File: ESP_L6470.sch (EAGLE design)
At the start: 33 parts, among them J2 POWER_JACKPTH_LOCK, Q1 600mA/40V, Q2 600mA/40V, U1 L6470, U2 ESP-WROOM-03, U3 WS2811

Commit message: Update schematic with USB to Serial
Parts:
- removed U3: WS2811, SparkFun-LED:LED-TRICOLOR-5050-ICWS2811
- added C9: 10uF, microbuilder:CAP_CERAMIC0805-NOOUTLINE
- added D2: RED, microbuilder:LED0805_NOOUTLINE
- added D3: GREEN, microbuilder:LED0805_NOOUTLINE
- added IC2: CP2104, microbuilder:CP2104
- added JP2, JP3: JUMPER-SMT_2_NC_TRACE_NO-SILK, SparkFun-Jumpers:JUMPER-SMT_2_NC_TRACE_NO-SILK
- added R3, R4: 1K, microbuilder:RESISTOR0805_NOOUTLINE
- added X1: 20329, microbuilder:USB_MICRO_20329_V2
- C7: value 0.1uF -> 10uF; device SparkFun-Capacitors:0.1UF-25V(+80/-20%)(0603) -> microbuilder:CAP_CERAMIC0805-NOOUTLINE
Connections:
- net MC_EN renamed RESET
- new net N$1: U2.IO25
- new net N$10: U2.SDI
- new net N$13: IC2G$1.D+, X1.D+
- new net N$14: IC2G$1.D-, X1.D-
- new net N$15: C7.1, IC2G$1.VPP
- new net N$16: D2.A, R3.1
- new net N$17: D3.A, R4.1
- new net N$18: D2.C, IC2G$1.GPIO0/TXLED
- new net N$19: D3.C, IC2G$1.GPIO1/RXLED
- new net N$2: U2.SHD
- new net N$3: U2.SWP
- new net N$4: U2.SCS
- new net N$5: U2.SCK
- new net N$6: U2.SDO
- new net RXD0: IC2G$1.TXD, JP2.1
- new net TXD0: IC2G$1.RXD, JP3.1
- new net VBUS: IC2G$1.VBUS, X1.VBUS
- net 3.3V: now also C9.1, IC2G$1.REGIN, IC2G$1.VDD, IC2G$1.VIO, R3.2, R4.2; no longer C7.1, U3.VDD
- net DTR: now also IC2G$1.DTR
- net GND: now also C9.2, IC2G$1.GND, X1.GND; no longer U3.VSS
- net NEOPIXEL: no longer U3.DI
- net PGND: now also J2.GND, J2.GNDBREAK; no longer J2.PWR
- net RTS: now also IC2G$1.RTS
- net RX: now also JP3.2
- net TX: now also JP2.2
- net VS: now also J2.PWR; no longer J2.GND, J2.GNDBREAK
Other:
- note added: "CP2105 usb to serial"
- note added: "PHYSICAL INTERFACE"
- note added: "POWER JACK"
- note added: "TO STEPER"
- note added: "USB TO SERIAL CONVERTER"
- note removed: "INTERFACE"
- note removed: "SJ1 allows user to select external power over comm headers or internal 3.3V power. NB- DO NOT connect external power to JP1 or JP2 when internal supply is selected!"
- note removed: "SJ3 allows you to route the SDO (serial data out) either to the next board (if this board is in a chain) or back to the previous board (if this board is the last or only board in the chain). It defaults to back to previous board, for single board applications."
- note removed: "Supply Connector"
- note removed: "Vs must be between 8V and 45V Motor supply must be enabled for chip comms to work!"
- moved on the sheet: C7, J2, PROGRAMMER

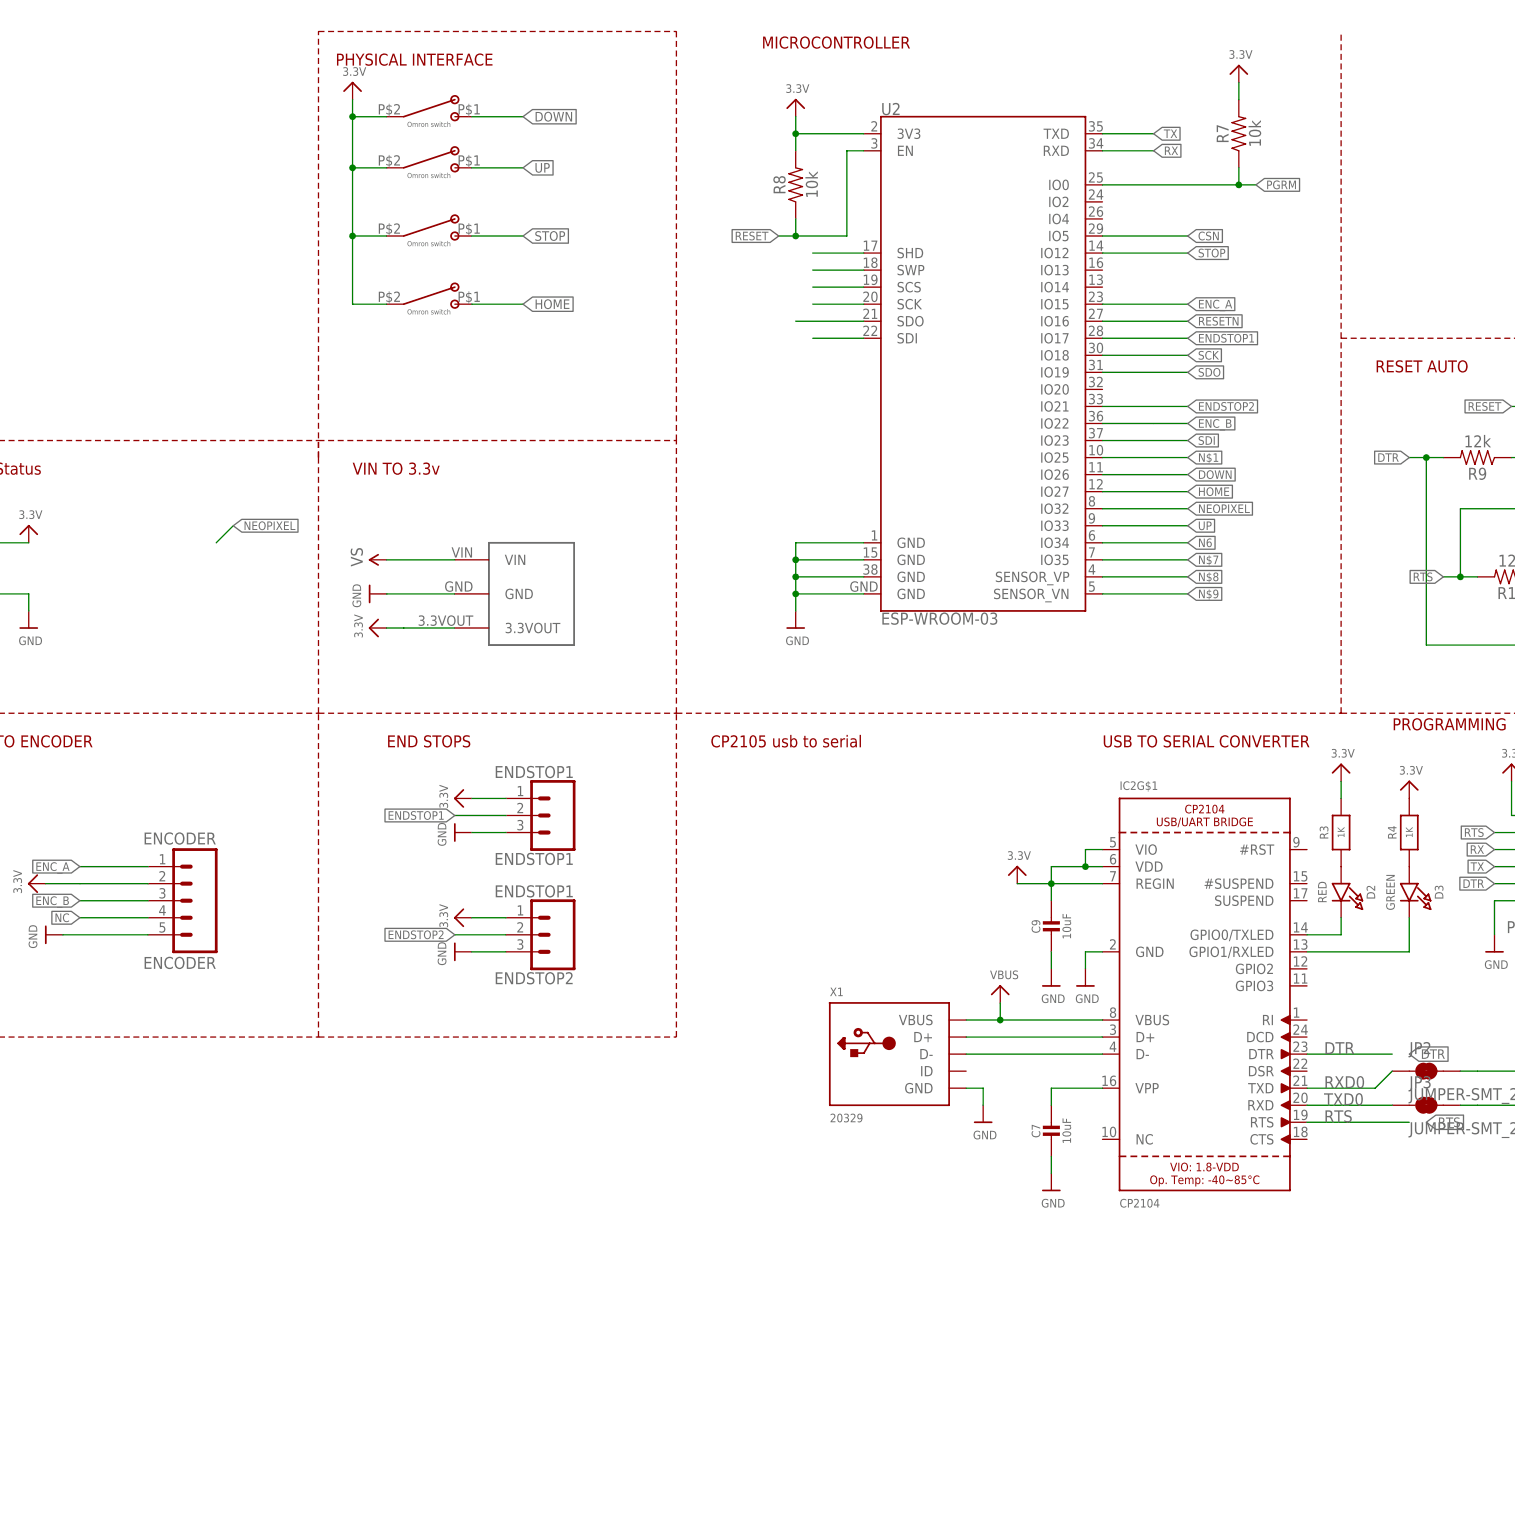
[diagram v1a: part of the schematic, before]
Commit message: added some components
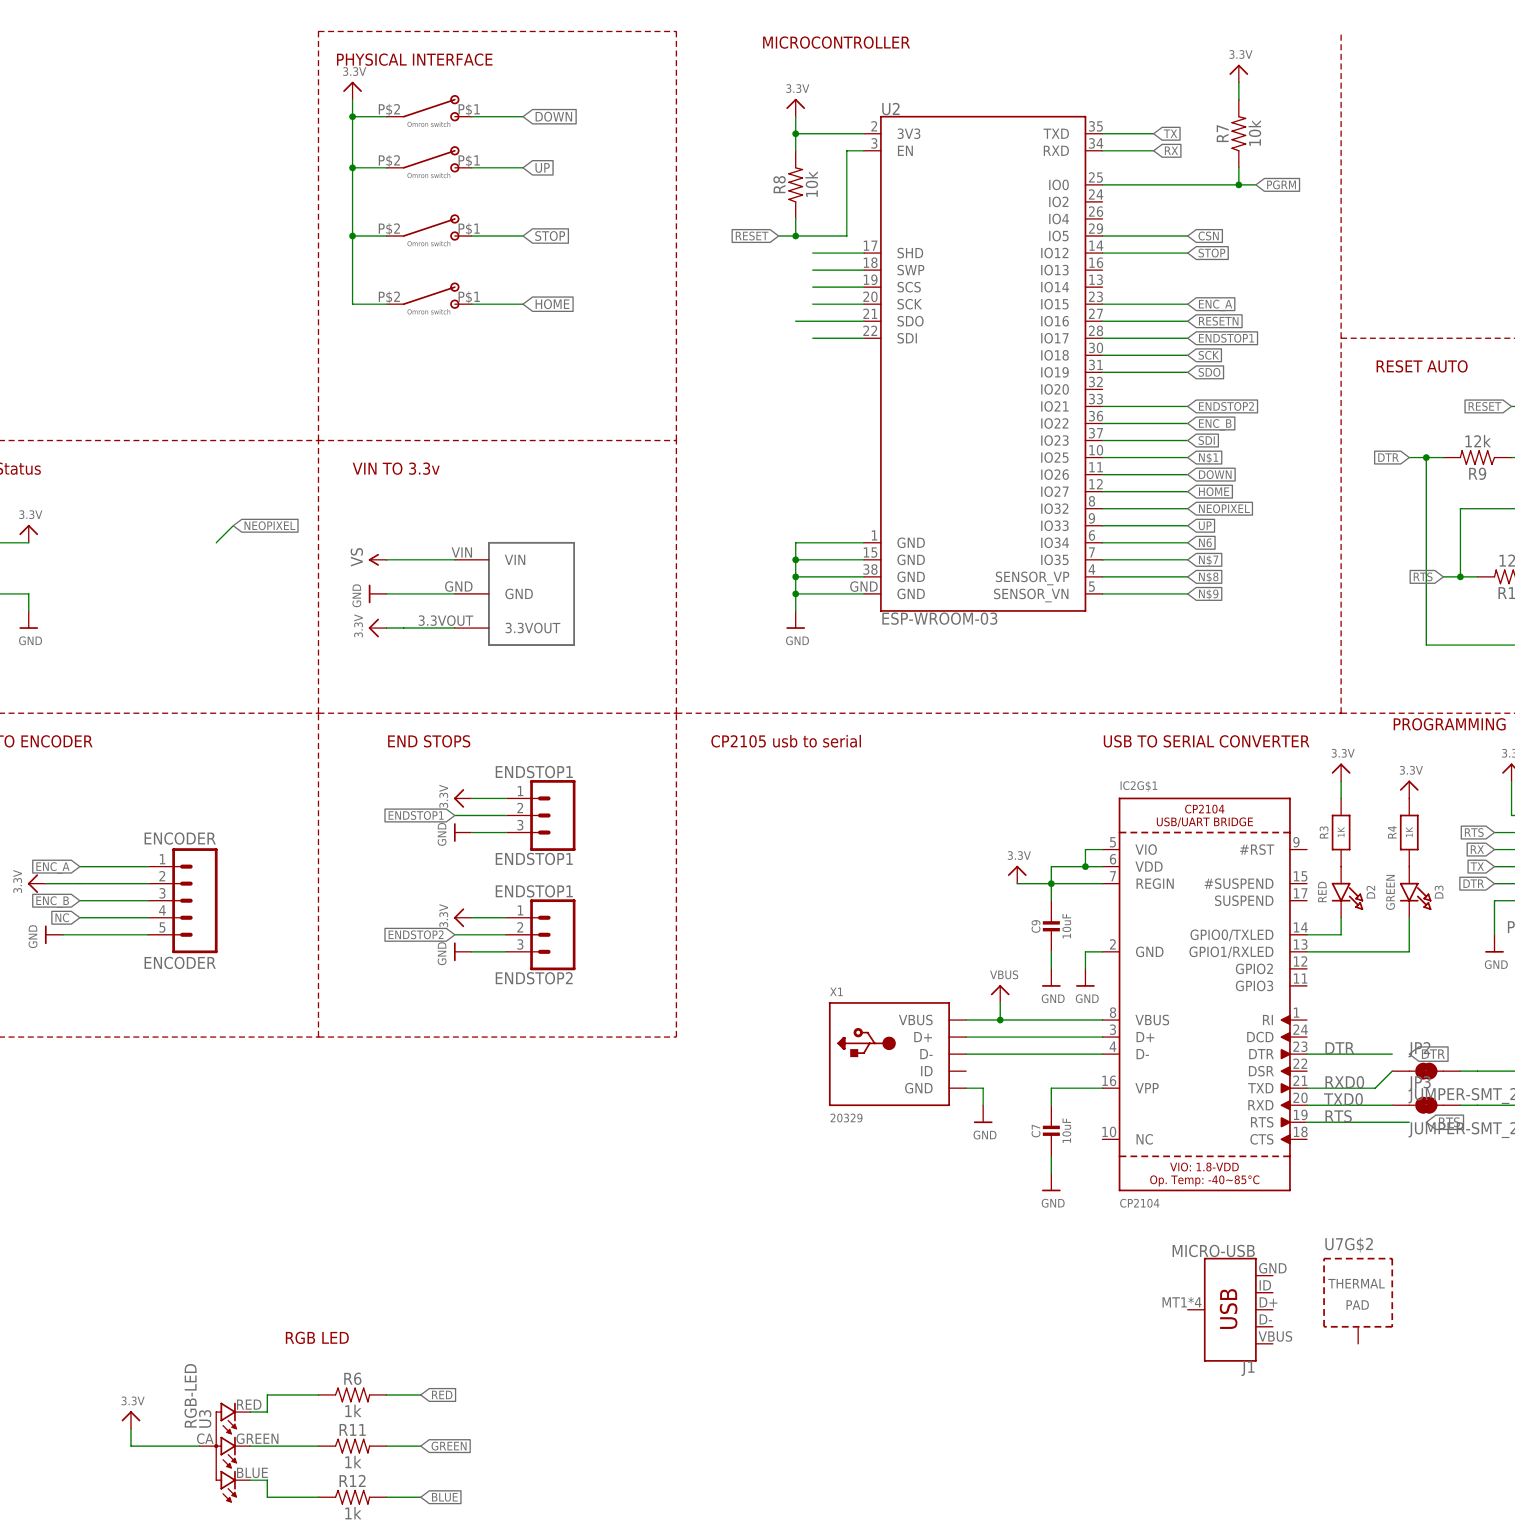
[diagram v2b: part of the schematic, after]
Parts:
- added J1: MICRO-USB, SparkFun-Connectors:USB_MICRO-B_SMT
- added R11, R12, R6: 1k, SparkFun-Resistors:1KOHM-0603-1/10W-1%
- added U3: RGB-LED, Particle:RGB-LED-CLMVB-FKARGB
- added U7: CP2104, microbuilder:CP2104
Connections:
- new net BLUE: R12.2
- new net GREEN: R11.2
- new net N$11: R11.1, U3.3
- new net N$12: R6.1, U3.4
- new net N$20: R12.1, U3.2
- new net RED: R6.2
- net 3.3V: now also U3.1
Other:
- note added: "RGB LED"
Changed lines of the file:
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@@
 <layer number="59" name="tCarbon" color="7" fill="1" visible="no" active="no"/>
 <layer number="60" name="bCarbon" color="7" fill="1" visible="no" active="no"/>
+<layer number="88" name="SimResults" color="9" fill="1" visible="yes" active="yes"/>
+<layer number="89" name="SimProbes" color="9" fill="1" visible="yes" active="yes"/>
 <layer number="90" name="Modules" color="5" fill="1" visible="yes" active="yes"/>
 <layer number="91" name="Nets" color="2" fill="1" visible="yes" active="yes"/>
@@
 <part name="JP2" library="SparkFun-Jumpers" deviceset="JUMPER-SMT_2_NC_TRACE" device="_NO-SILK"/>
 <part name="JP3" library="SparkFun-Jumpers" deviceset="JUMPER-SMT_2_NC_TRACE" device="_NO-SILK"/>
+<part name="U7" library="microbuilder" deviceset="CP2104" device="" value="CP2104"/>
+<part name="J1" library="SparkFun-Connectors" deviceset="USB_MICRO-B" device="_SMT" value="MICRO-USB"/>
+<part name="U3" library="Particle" deviceset="RGB-LED-CLMVB-FKA" device="RGB" value="RGB-LED"/>
+<part name="U$26" library="microbuilder" deviceset="3.3V" device=""/>
+<part name="R6" library="SparkFun-Resistors" deviceset="1KOHM" device="-0603-1/10W-1%" value="1k"/>
+<part name="R11" library="SparkFun-Resistors" deviceset="1KOHM" device="-0603-1/10W-1%" value="1k"/>
+<part name="R12" library="SparkFun-Resistors" deviceset="1KOHM" device="-0603-1/10W-1%" value="1k"/>
 </parts>
 <sheets>
@@
 <text x="304.8" y="116.84" size="1.778" layer="94">VIN TO 3.3v</text>
 <wire x1="299.72" y1="33.02" x2="299.72" y2="81.28" width="0.1524" layer="94" style="shortdash"/>
-<wire x1="299.72" y1="81.28" x2="299.72" y2="119.38" width="0.1524" layer="94" style="shortdash"/>
+<wire x1="299.72" y1="81.28" x2="299.72" y2="121.92" width="0.1524" layer="94" style="shortdash"/>
 <text x="251.46" y="76.2" size="1.778" layer="94">TO ENCODER</text>
-<wire x1="299.72" y1="119.38" x2="299.72" y2="121.92" width="0.1524" layer="94" style="shortdash"/>
 <wire x1="299.72" y1="33.02" x2="353.06" y2="33.02" width="0.1524" layer="94" style="shortdash"/>
 <wire x1="246.38" y1="81.28" x2="246.38" y2="121.92" width="0.1524" layer="94" style="shortdash"/>
@@
 <text x="251.46" y="116.84" size="1.778" layer="94">Status</text>
 <wire x1="299.72" y1="182.88" x2="353.06" y2="182.88" width="0.1524" layer="94" style="shortdash"/>
-<wire x1="299.72" y1="119.38" x2="299.72" y2="182.88" width="0.1524" layer="94" style="shortdash"/>
+<wire x1="299.72" y1="121.92" x2="299.72" y2="182.88" width="0.1524" layer="94" style="shortdash"/>
 <text x="302.26" y="177.8" size="1.778" layer="94">PHYSICAL INTERFACE</text>
 <text x="358.14" y="76.2" size="1.778" layer="94">CP2105 usb to serial</text>
@@
 <text x="86.36" y="157.48" size="1.778" layer="94">TO ENCODER</text>
 <text x="416.56" y="76.2" size="1.778" layer="94">USB TO SERIAL CONVERTER</text>
+<text x="294.64" y="-12.7" size="1.778" layer="94">RGB LED</text>
 </plain>
 <instances>
@@
 <instance part="JP2" gate="G$1" x="464.82" y="27.94"/>
 <instance part="JP3" gate="G$1" x="464.82" y="22.86"/>
+<instance part="U7" gate="G$2" x="454.66" y="-5.08"/>
+<instance part="J1" gate="G$1" x="436.88" y="-7.62" rot="R180"/>
+<instance part="U3" gate="G$1" x="284.48" y="-27.94" rot="R90"/>
+<instance part="U$26" gate="G$1" x="271.78" y="-22.86"/>
+<instance part="R6" gate="G$1" x="304.8" y="-20.32"/>
+<instance part="R11" gate="G$1" x="304.8" y="-27.94"/>
+<instance part="R12" gate="G$1" x="304.8" y="-35.56"/>
 </instances>
 <busses>
@@
 <pinref part="U$30" gate="G$1" pin="3.3V"/>
 </segment>
+<segment>
+<pinref part="U3" gate="G$1" pin="1"/>
+<wire x1="281.94" y1="-27.94" x2="271.78" y2="-27.94" width="0.1524" layer="91"/>
+<pinref part="U$26" gate="G$1" pin="3.3V"/>
+<wire x1="271.78" y1="-27.94" x2="271.78" y2="-25.4" width="0.1524" layer="91"/>
+</segment>
 </net>
 <net name="OSCIN" class="0">
@@
 </segment>
 </net>
+<net name="RED" class="0">
+<segment>
+<pinref part="R6" gate="G$1" pin="2"/>
+<wire x1="309.88" y1="-20.32" x2="314.96" y2="-20.32" width="0.1524" layer="91"/>
+<label x="314.96" y="-20.32" size="1.27" layer="95" xref="yes"/>
+</segment>
+</net>
+<net name="GREEN" class="0">
+<segment>
+<pinref part="R11" gate="G$1" pin="2"/>
+<wire x1="309.88" y1="-27.94" x2="314.96" y2="-27.94" width="0.1524" layer="91"/>
+<label x="314.96" y="-27.94" size="1.27" layer="95" xref="yes"/>
+</segment>
+</net>
+<net name="BLUE" class="0">
+<segment>
+<pinref part="R12" gate="G$1" pin="2"/>
+<wire x1="309.88" y1="-35.56" x2="314.96" y2="-35.56" width="0.1524" layer="91"/>
+<label x="314.96" y="-35.56" size="1.27" layer="95" xref="yes"/>
+</segment>
+</net>
+<net name="N$11" class="0">
+<segment>
+<pinref part="U3" gate="G$1" pin="3"/>
+<wire x1="289.56" y1="-27.94" x2="299.72" y2="-27.94" width="0.1524" layer="91"/>
+<pinref part="R11" gate="G$1" pin="1"/>
+</segment>
+</net>
+<net name="N$12" class="0">
+<segment>
+<pinref part="U3" gate="G$1" pin="4"/>
+<wire x1="289.56" y1="-22.86" x2="292.1" y2="-22.86" width="0.1524" layer="91"/>
+<wire x1="292.1" y1="-22.86" x2="292.1" y2="-20.32" width="0.1524" layer="91"/>
+<pinref part="R6" gate="G$1" pin="1"/>
+<wire x1="292.1" y1="-20.32" x2="299.72" y2="-20.32" width="0.1524" layer="91"/>
+</segment>
+</net>
+<net name="N$20" class="0">
+<segment>
+<pinref part="R12" gate="G$1" pin="1"/>
+<wire x1="299.72" y1="-35.56" x2="292.1" y2="-35.56" width="0.1524" layer="91"/>
+<wire x1="292.1" y1="-35.56" x2="292.1" y2="-33.02" width="0.1524" layer="91"/>
+<pinref part="U3" gate="G$1" pin="2"/>
+<wire x1="292.1" y1="-33.02" x2="289.56" y2="-33.02" width="0.1524" layer="91"/>
+</segment>
+</net>

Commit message: update with USB to Serial
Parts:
- removed C7, C9: 10uF, microbuilder:CAP_CERAMIC0805-NOOUTLINE
- removed D2: RED, microbuilder:LED0805_NOOUTLINE
- removed D3: GREEN, microbuilder:LED0805_NOOUTLINE
- removed JP1: JUMPER-SMT_2_NC_TRACE_NO-SILK, SparkFun-Jumpers:JUMPER-SMT_2_NC_TRACE_NO-SILK
- removed PROGRAMMER: (no value), SparkFun-Connectors:CONN_06NO_SILK_NO_POP
- removed R3, R4: 1K, microbuilder:RESISTOR0805_NOOUTLINE
- removed U7: CP2104, microbuilder:CP2104
- removed X1: 20329, microbuilder:USB_MICRO_20329_V2
- C1: device SparkFun-Capacitors:0.1UF-25V(+80/-20%)(0603) -> SparkFun-Passives:CAP0603-CAP
- C4, C5: device SparkFun-Capacitors:0.22UF50V-20%,+80%(0603) -> SparkFun-Passives:CAP0603-CAP
- R1, R2: device SparkFun-Resistors:10KOHM1/10W1%(0603)0603 -> SparkFun-Passives:RESISTOR0603-RES
- R10, R7, R8, R9: device SparkFun-Resistors:RESISTOR0805 -> SparkFun-Passives:RESISTOR0603-RES
- R11, R12, R6: device SparkFun-Resistors:1KOHM-0603-1/10W-1% -> SparkFun-Passives:RESISTOR0603-RES
- R5: device SparkFun-Resistors:8.2KOHM-1/10W-5%(0603) -> SparkFun-Passives:RESISTOR0603-RES
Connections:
- removed net N$15: C7.1, IC2G$1.VPP
- removed net N$16: D2.A, R3.1
- removed net N$17: D3.A, R4.1
- removed net N$18: D2.C, IC2G$1.GPIO0/TXLED
- removed net N$19: D3.C, IC2G$1.GPIO1/RXLED
- removed net N$7: U2.IO35
- removed net N6: U2.IO34
- removed net NEOPIXEL: U2.IO32
- removed net PGND: C3.-, C4.2, J2.GND, J2.GNDBREAK, JP1.2
- new net N$100: U2.IO13
- new net N$101: U2.IO20
- net 3.3V: no longer C9.1, PROGRAMMER.1, R3.2, R4.2
- net BLUE: now also IC2G$1.GPIO1/RXLED, U2.IO35
- net DTR: no longer PROGRAMMER.5
- net ENC_A: now also U2.IO21; no longer U2.IO15
- net ENDSTOP1: now also U2.IO15; no longer U2.IO17
- net ENDSTOP2: now also U2.IO17; no longer U2.IO21
- net GND: now also C3.-, C4.2, J1.GND, J2.GND, J2.GNDBREAK; no longer C7.2, C9.2, JP1.1, PROGRAMMER.6, X1.GND
- net GREEN: now also IC2G$1.GPIO0/TXLED, U2.IO34
- net N$13: now also J1.D+; no longer X1.D+
- net N$14: now also J1.D-; no longer X1.D-
- net RED: now also U2.IO32
- net RTS: no longer PROGRAMMER.2
- net RX: no longer PROGRAMMER.3
- net TX: no longer PROGRAMMER.4
- net VBUS: now also J1.VBUS; no longer X1.VBUS
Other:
- moved on the sheet: J1, R11, R12, R6, U3

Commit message: Updated board
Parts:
- added U$13: INTERFACE_NETSTEPPER, IAD_GRAPHIC:INTERFACE_NETSTEPPER
- added U$15: ZHDK_LOGO_METAL, IAD_GRAPHIC:ZHDK_LOGO_METAL
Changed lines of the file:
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@@
 <part name="R11" library="SparkFun-Passives" deviceset="RESISTOR" device="0603-RES" value="1k"/>
 <part name="R12" library="SparkFun-Passives" deviceset="RESISTOR" device="0603-RES" value="1k"/>
+<part name="U$13" library="IAD_GRAPHIC" deviceset="INTERFACE_NETSTEPPER" device=""/>
+<part name="U$15" library="IAD_GRAPHIC" deviceset="ZHDK_LOGO_METAL" device=""/>
 </parts>
 <sheets>
@@
 <instance part="R11" gate="G$1" x="279.4" y="99.06"/>
 <instance part="R12" gate="G$1" x="279.4" y="91.44"/>
+<instance part="U$13" gate="G$1" x="251.46" y="127"/>
+<instance part="U$15" gate="G$1" x="254" y="134.62"/>
 </instances>
 <busses>
